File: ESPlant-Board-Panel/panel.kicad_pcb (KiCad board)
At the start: 4 copper layers, 64 x 116 mm, 150 parts, among them J1 Conn_01x05, U1 USB-C, U13 ESP32-C6-MINI-1-N4, U3 AHT20-F, U4 Tactile-Switch, U5 3.3V-Regulator, U6 Light sensor, U7 Tactile-Switch, U8 Slide-Switch, U9 Battery-Spring

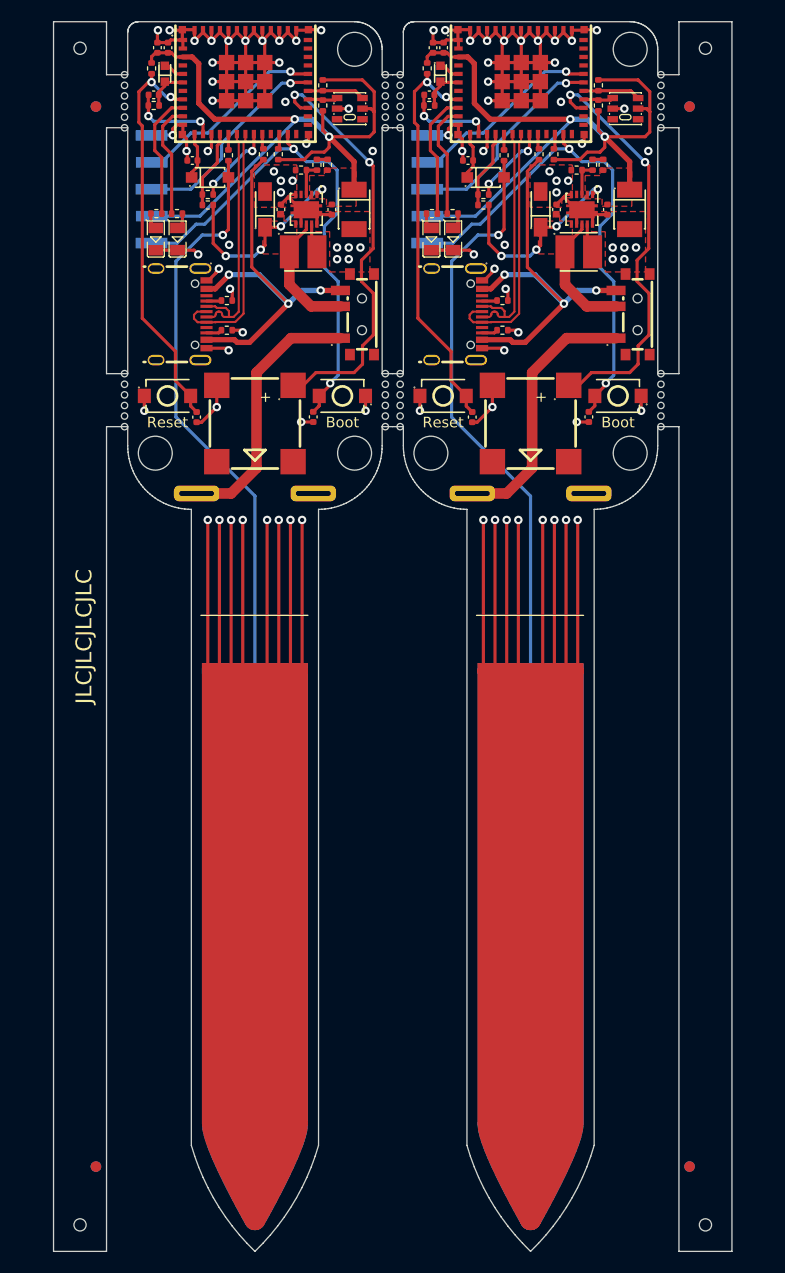
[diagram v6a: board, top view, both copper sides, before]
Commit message: Panel: Make board width be 70mm
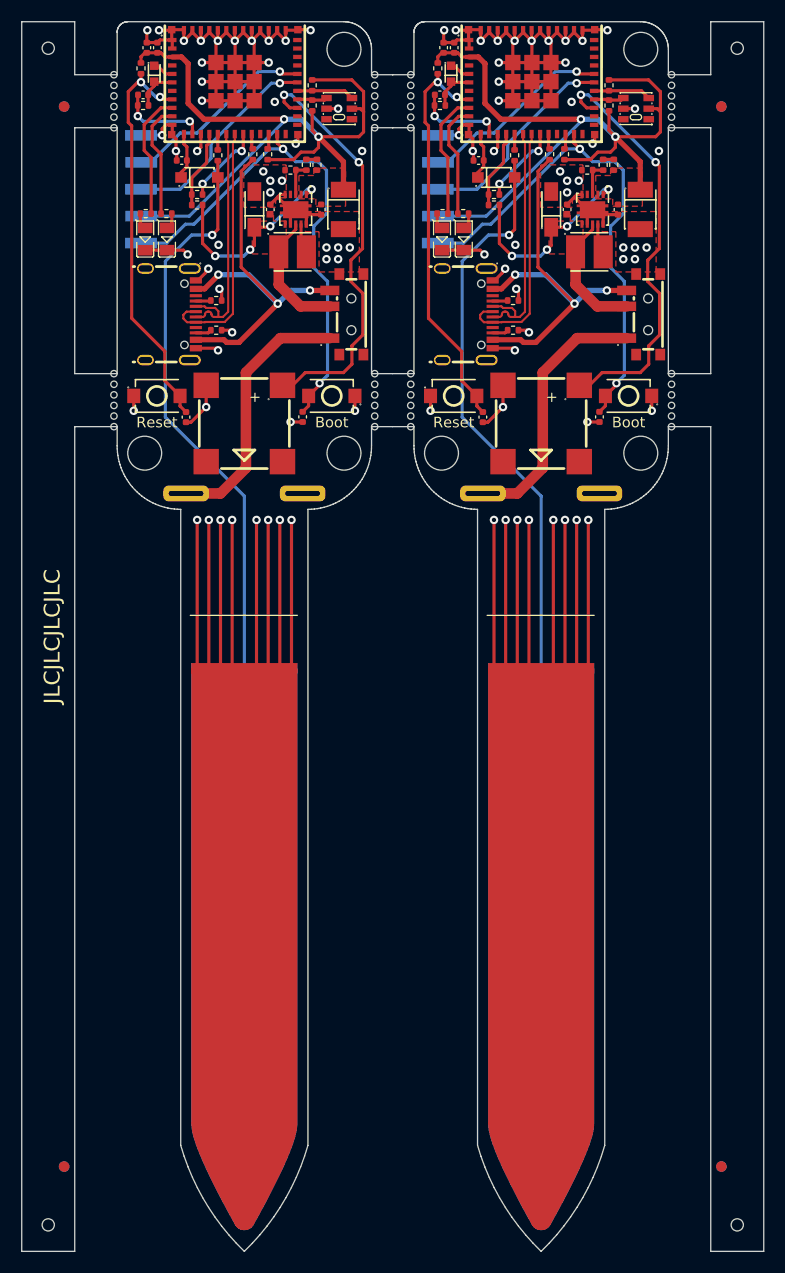
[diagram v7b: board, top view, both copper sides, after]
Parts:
- removed the BZ1 at (212.0, 57.9)
- removed the BZ1 at (238.0, 57.9)
- removed the C1 at (245.3, 37.7)
- removed the C1 at (219.3, 37.7)
- removed the C10 at (239.0, 37.7)
- removed the C10 at (213.0, 37.7)
- removed the C11 at (232.5, 57.3)
- removed the C11 at (206.5, 57.3)
- removed the C2 at (221.4, 37.7)
- removed the C2 at (247.4, 37.7)
- removed the C3 at (232.1, 33.1)
- removed the C3 at (206.1, 33.1)
- removed the C4 at (238.0, 81.0)
- removed the C4 at (212.0, 81.0)
- removed the C5 at (243.5, 57.3)
- removed the C5 at (217.5, 57.3)
- removed the C6 at (214.5, 37.7)
- removed the C6 at (240.5, 37.7)
- removed the C7 at (202.5, 26.9)
- removed the C7 at (228.5, 26.9)
- removed the C8 at (203.8, 22.4)
- removed the C8 at (229.8, 22.4)
- removed the C9 at (228.8, 22.4)
- removed the C9 at (202.8, 22.4)
- removed the D1 at (204.7, 40.5)
- removed the D1 at (230.7, 40.5)
- removed the D2 at (207.8, 34.7)
- removed the D2 at (233.8, 34.7)
- removed the D3 at (228.7, 40.5)
- removed the D3 at (202.7, 40.5)
- removed the H1 at (221.4, 22.6)
- removed the H1 at (247.4, 22.6)
- removed the H2 at (228.6, 60.7)
- removed the H2 at (202.6, 60.7)
- removed the H3 at (247.4, 60.7)
- removed the H3 at (221.4, 60.7)
- removed the J1 at (227.0, 35.8)
- removed the J1 at (201.0, 35.8)
- removed the L1 at (216.6, 41.7)
- removed the L1 at (242.6, 41.7)
- removed the R1 at (244.9, 33.5)
- removed the R1 at (218.9, 33.5)
- removed the R10 at (244.4, 27.9)
- removed the R10 at (218.4, 27.9)
- removed the R11 at (209.4, 46.3)
- removed the R11 at (235.4, 46.3)
- removed the R12 at (235.4, 49.1)
- removed the R12 at (209.4, 49.1)
- removed the R13 at (230.7, 38.1)
- removed the R13 at (204.7, 38.1)
- removed the R14 at (202.7, 38.1)
- removed the R14 at (228.7, 38.1)
- removed the R15 at (243.9, 33.5)
- removed the R15 at (217.9, 33.5)
- removed the R16 at (216.4, 34.0)
- removed the R16 at (242.4, 34.0)
- removed the R2 at (218.4, 26.0)
- removed the R2 at (244.4, 26.0)
- removed the R3 at (202.5, 27.9)
- removed the R3 at (228.5, 27.9)
- removed the R4 at (207.6, 37.3)
- removed the R4 at (233.6, 37.3)
- removed the R5 at (240.2, 32.5)
- removed the R5 at (214.2, 32.5)
- removed the R6 at (233.6, 36.3)
- removed the R6 at (207.6, 36.3)
- removed the R7 at (238.8, 32.5)
- removed the R7 at (212.8, 32.5)
- removed the R8 at (209.5, 32.6)
- removed the R8 at (235.5, 32.6)
- removed the R9 at (228.3, 24.4)
- removed the R9 at (202.3, 24.4)
- removed the U1 at (205.1, 47.6)
- removed the U1 at (231.1, 47.6)
- removed the U13 at (237.1, 25.7)
- removed the U13 at (211.1, 25.7)
- removed the U3 at (221.0, 28.2)
- removed the U3 at (247.0, 28.2)
- removed the U4 at (229.8, 55.3)
- removed the U4 at (203.8, 55.3)
- removed the U5 at (216.9, 37.7)
- removed the U5 at (242.9, 37.7)
- removed the U6 at (229.5, 24.9)
- removed the U6 at (203.5, 24.9)
- removed the U7 at (246.3, 55.3)
- removed the U7 at (220.3, 55.3)
- removed the U8 at (221.7, 47.6)
- removed the U8 at (247.7, 47.6)
- removed the U9 at (238.0, 64.5)
- removed the U9 at (212.0, 64.5)
- added BZ1: Buzzer, CustomFootprints:BUZ-SMD_4P-L8.5-W8.5-P8.50-BR, F.Cu at (211.0, 57.9)
- added BZ1: Buzzer, CustomFootprints:BUZ-SMD_4P-L8.5-W8.5-P8.50-BR, F.Cu at (239.0, 57.9)
- added C1: 2.2uF-Ceramic, Capacitor_SMD:C_0402_1005Metric, F.Cu at (246.3, 37.7)
- added C1: 2.2uF-Ceramic, Capacitor_SMD:C_0402_1005Metric, F.Cu at (218.3, 37.7)
- added C10: 10uF-Tantalum, CustomFootprints:CAP-SMD_L3.2-W1.6-RD-C7171, F.Cu at (212.0, 37.7)
- added C10: 10uF-Tantalum, CustomFootprints:CAP-SMD_L3.2-W1.6-RD-C7171, F.Cu at (240.0, 37.7)
- added C11: 100nF-Ceramic, Capacitor_SMD:C_0402_1005Metric, F.Cu at (205.5, 57.3)
- added C11: 100nF-Ceramic, Capacitor_SMD:C_0402_1005Metric, F.Cu at (233.5, 57.3)
- added C2: 100uF-Tantalum, CustomFootprints:CASE-B_3528, F.Cu at (220.4, 37.7)
- added C2: 100uF-Tantalum, CustomFootprints:CASE-B_3528, F.Cu at (248.4, 37.7)
- added C3: 10nF, Capacitor_SMD:C_0402_1005Metric, F.Cu at (205.1, 33.1)
- added C3: 10nF, Capacitor_SMD:C_0402_1005Metric, F.Cu at (233.1, 33.1)
- added C4: 7pF-27pF, A=2.75cm^2, CustomFootprints:Sensor-Tip, B.Cu at (211.0, 81.0)
- added C4: 7pF-27pF, A=2.75cm^2, CustomFootprints:Sensor-Tip, B.Cu at (239.0, 81.0)
- added C5: 100nF-Ceramic, Capacitor_SMD:C_0402_1005Metric, F.Cu at (244.5, 57.3)
- added C5: 100nF-Ceramic, Capacitor_SMD:C_0402_1005Metric, F.Cu at (216.5, 57.3)
- added C6: 100nF-Ceramic, Capacitor_SMD:C_0402_1005Metric, F.Cu at (241.5, 37.7)
- added C6: 100nF-Ceramic, Capacitor_SMD:C_0402_1005Metric, F.Cu at (213.5, 37.7)
- added C7: 10uF, Capacitor_SMD:C_0402_1005Metric, F.Cu at (201.5, 26.9)
- added C7: 10uF, Capacitor_SMD:C_0402_1005Metric, F.Cu at (229.5, 26.9)
- added C8: 10nF, Capacitor_SMD:C_0402_1005Metric, F.Cu at (202.8, 22.4)
- added C8: 10nF, Capacitor_SMD:C_0402_1005Metric, F.Cu at (230.8, 22.4)
- added C9: 10uF, Capacitor_SMD:C_0402_1005Metric, F.Cu at (201.8, 22.4)
- added C9: 10uF, Capacitor_SMD:C_0402_1005Metric, F.Cu at (229.8, 22.4)
- added D1: GREEN, CustomFootprints:LED0805-R-RD, F.Cu at (231.7, 40.5)
- added D1: GREEN, CustomFootprints:LED0805-R-RD, F.Cu at (203.7, 40.5)
- added D2: Switching-Diode, CustomFootprints:SOD-123F_L2.7-W1.6-LS3.8-RD, F.Cu at (234.8, 34.7)
- added D2: Switching-Diode, CustomFootprints:SOD-123F_L2.7-W1.6-LS3.8-RD, F.Cu at (206.8, 34.7)
- added D3: RED, CustomFootprints:LED0805-R-RD, F.Cu at (229.7, 40.5)
- added D3: RED, CustomFootprints:LED0805-R-RD, F.Cu at (201.7, 40.5)
- added H1: MountingHole, MountingHole:MountingHole_3.2mm_M3, F.Cu at (248.4, 22.6)
- added H1: MountingHole, MountingHole:MountingHole_3.2mm_M3, F.Cu at (220.4, 22.6)
- added H2: MountingHole, MountingHole:MountingHole_3.2mm_M3, F.Cu at (201.6, 60.7)
- added H2: MountingHole, MountingHole:MountingHole_3.2mm_M3, F.Cu at (229.6, 60.7)
- added H3: MountingHole, MountingHole:MountingHole_3.2mm_M3, F.Cu at (248.4, 60.7)
- added H3: MountingHole, MountingHole:MountingHole_3.2mm_M3, F.Cu at (220.4, 60.7)
- added J1: Conn_01x05, CustomFootprints:PinHeader_1x05_P2.54mm_Vertical_SMD, B.Cu at (228.0, 35.8)
- added J1: Conn_01x05, CustomFootprints:PinHeader_1x05_P2.54mm_Vertical_SMD, B.Cu at (200.0, 35.8)
- added L1: 6.8uH, CustomFootprints:IND-SMD_L3.5-W3.0, F.Cu at (243.6, 41.7)
- added L1: 6.8uH, CustomFootprints:IND-SMD_L3.5-W3.0, F.Cu at (215.6, 41.7)
- added R1: 100k, Resistor_SMD:R_0402_1005Metric, F.Cu at (245.9, 33.5)
- added R1: 100k, Resistor_SMD:R_0402_1005Metric, F.Cu at (217.9, 33.5)
- added R10: 5k1, Resistor_SMD:R_0402_1005Metric, F.Cu at (245.4, 27.9)
- added R10: 5k1, Resistor_SMD:R_0402_1005Metric, F.Cu at (217.4, 27.9)
- added R11: 5k1, Resistor_SMD:R_0402_1005Metric, F.Cu at (208.4, 46.3)
- added R11: 5k1, Resistor_SMD:R_0402_1005Metric, F.Cu at (236.4, 46.3)
- added R12: 5k1, Resistor_SMD:R_0402_1005Metric, F.Cu at (236.4, 49.1)
- added R12: 5k1, Resistor_SMD:R_0402_1005Metric, F.Cu at (208.4, 49.1)
- added R13: 120, Resistor_SMD:R_0402_1005Metric, F.Cu at (231.7, 38.1)
- added R13: 120, Resistor_SMD:R_0402_1005Metric, F.Cu at (203.7, 38.1)
- added R14: 120, Resistor_SMD:R_0402_1005Metric, F.Cu at (201.7, 38.1)
- added R14: 120, Resistor_SMD:R_0402_1005Metric, F.Cu at (229.7, 38.1)
- added R15: 1M, Resistor_SMD:R_0402_1005Metric, F.Cu at (244.9, 33.5)
- added R15: 1M, Resistor_SMD:R_0402_1005Metric, F.Cu at (216.9, 33.5)
- added R16: 200k, Resistor_SMD:R_0402_1005Metric, F.Cu at (215.4, 34.0)
- added R16: 200k, Resistor_SMD:R_0402_1005Metric, F.Cu at (243.4, 34.0)
- added R2: 5k1, Resistor_SMD:R_0402_1005Metric, F.Cu at (217.4, 26.0)
- added R2: 5k1, Resistor_SMD:R_0402_1005Metric, F.Cu at (245.4, 26.0)
- added R3: 47k, Resistor_SMD:R_0402_1005Metric, F.Cu at (229.5, 27.9)
- added R3: 47k, Resistor_SMD:R_0402_1005Metric, F.Cu at (201.5, 27.9)
- added R4: 5k1, Resistor_SMD:R_0402_1005Metric, F.Cu at (234.6, 37.3)
- added R4: 5k1, Resistor_SMD:R_0402_1005Metric, F.Cu at (206.6, 37.3)
- added R5: 10k, Resistor_SMD:R_0402_1005Metric, F.Cu at (213.2, 32.5)
- added R5: 10k, Resistor_SMD:R_0402_1005Metric, F.Cu at (241.2, 32.5)
- added R6: 2k, Resistor_SMD:R_0402_1005Metric, F.Cu at (234.6, 36.3)
- added R6: 2k, Resistor_SMD:R_0402_1005Metric, F.Cu at (206.6, 36.3)
- added R7: 10k, Resistor_SMD:R_0402_1005Metric, F.Cu at (211.8, 32.5)
- added R7: 10k, Resistor_SMD:R_0402_1005Metric, F.Cu at (239.8, 32.5)
- added R8: 10k, Resistor_SMD:R_0402_1005Metric, F.Cu at (208.5, 32.6)
- added R8: 10k, Resistor_SMD:R_0402_1005Metric, F.Cu at (236.5, 32.6)
- added R9: 10k, Resistor_SMD:R_0402_1005Metric, F.Cu at (229.3, 24.4)
- added R9: 10k, Resistor_SMD:R_0402_1005Metric, F.Cu at (201.3, 24.4)
- added U1: USB-C, CustomFootprints:USB-C-SMD_G-SWITCH_GT-USB-7010EN, F.Cu at (232.1, 47.6)
- added U1: USB-C, CustomFootprints:USB-C-SMD_G-SWITCH_GT-USB-7010EN, F.Cu at (204.1, 47.6)
- added U13: ESP32-C6-MINI-1-N4, CustomFootprints:WIFIM-SMD_61P-L16.6-W13.2-P0.80-ESP32-C6-MINI-1-N4, F.Cu at (238.1, 25.7)
- added U13: ESP32-C6-MINI-1-N4, CustomFootprints:WIFIM-SMD_61P-L16.6-W13.2-P0.80-ESP32-C6-MINI-1-N4, F.Cu at (210.1, 25.7)
- added U3: AHT20-F, CustomFootprints:SENSOR-SMD-6_AHT20, F.Cu at (220.0, 28.2)
- added U3: AHT20-F, CustomFootprints:SENSOR-SMD-6_AHT20, F.Cu at (248.0, 28.2)
- added U4: Tactile-Switch, CustomFootprints:SW-SMD_L3.9-W3.0-P4.45, F.Cu at (230.8, 55.3)
- added U4: Tactile-Switch, CustomFootprints:SW-SMD_L3.9-W3.0-P4.45, F.Cu at (202.8, 55.3)
- added U5: 3.3V-Regulator, CustomFootprints:VSON-10_L3.0-W3.0-P0.50-BL-EP_TPS62410DRCR, F.Cu at (215.9, 37.7)
- added U5: 3.3V-Regulator, CustomFootprints:VSON-10_L3.0-W3.0-P0.50-BL-EP_TPS62410DRCR, F.Cu at (243.9, 37.7)
- added U6: Light sensor, CustomFootprints:SENSORS-SMD_ALS-PT19, F.Cu at (202.5, 24.9)
- added U6: Light sensor, CustomFootprints:SENSORS-SMD_ALS-PT19, F.Cu at (230.5, 24.9)
- added U7: Tactile-Switch, CustomFootprints:SW-SMD_L3.9-W3.0-P4.45, F.Cu at (247.3, 55.3)
- added U7: Tactile-Switch, CustomFootprints:SW-SMD_L3.9-W3.0-P4.45, F.Cu at (219.3, 55.3)
- added U8: Slide-Switch, CustomFootprints:SW-SMD_MK-12C02-G025, F.Cu at (220.7, 47.6)
- added U8: Slide-Switch, CustomFootprints:SW-SMD_MK-12C02-G025, F.Cu at (248.7, 47.6)
- added U9: Battery-Spring, CustomFootprints:AAA Battery-spring, B.Cu at (239.0, 64.5)
- added U9: Battery-Spring, CustomFootprints:AAA Battery-spring, B.Cu at (211.0, 64.5)
- moved KiKit_FID_B_2 3.00 mm to (256.0, 28.0)
- moved KiKit_FID_B_4 3.00 mm to (256.0, 128.0)
- moved KiKit_FID_T_2 3.00 mm to (256.0, 28.0)
- moved KiKit_FID_T_4 3.00 mm to (256.0, 128.0)
- moved KiKit_TO_2 3.00 mm to (257.5, 22.5)
- moved KiKit_TO_4 3.00 mm to (257.5, 133.5)
- moved KiKit_FID_B_1 3.00 mm to (194.0, 28.0)
- moved KiKit_FID_B_3 3.00 mm to (194.0, 128.0)
- moved KiKit_FID_T_1 3.00 mm to (194.0, 28.0)
- moved KiKit_FID_T_3 3.00 mm to (194.0, 128.0)
- moved KiKit_TO_1 3.00 mm to (192.5, 22.5)
- moved KiKit_TO_3 3.00 mm to (192.5, 133.5)
- moved KiKit_MB_1_1 1.00 mm to (223.3, 58.2)
- moved KiKit_MB_1_2 1.00 mm to (223.3, 57.2)
- moved KiKit_MB_1_3 1.00 mm to (223.3, 56.2)
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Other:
- board size 64 x 116 mm -> 70 x 116 mm

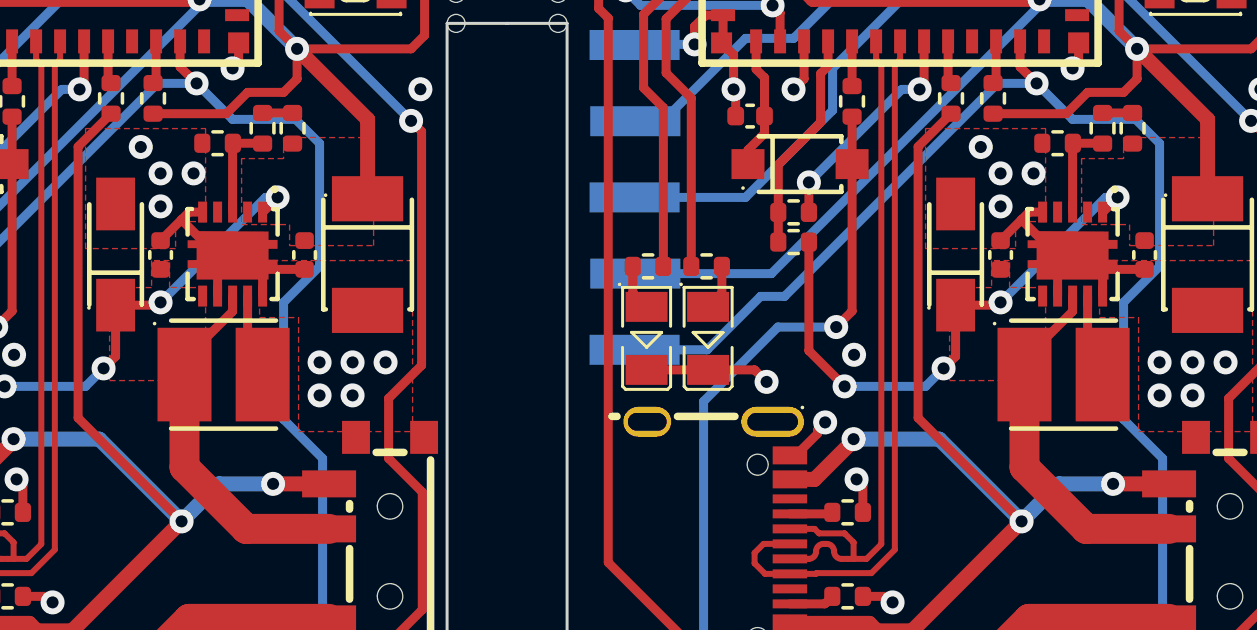
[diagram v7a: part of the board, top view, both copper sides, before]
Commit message: Board: Enable Power saving mode
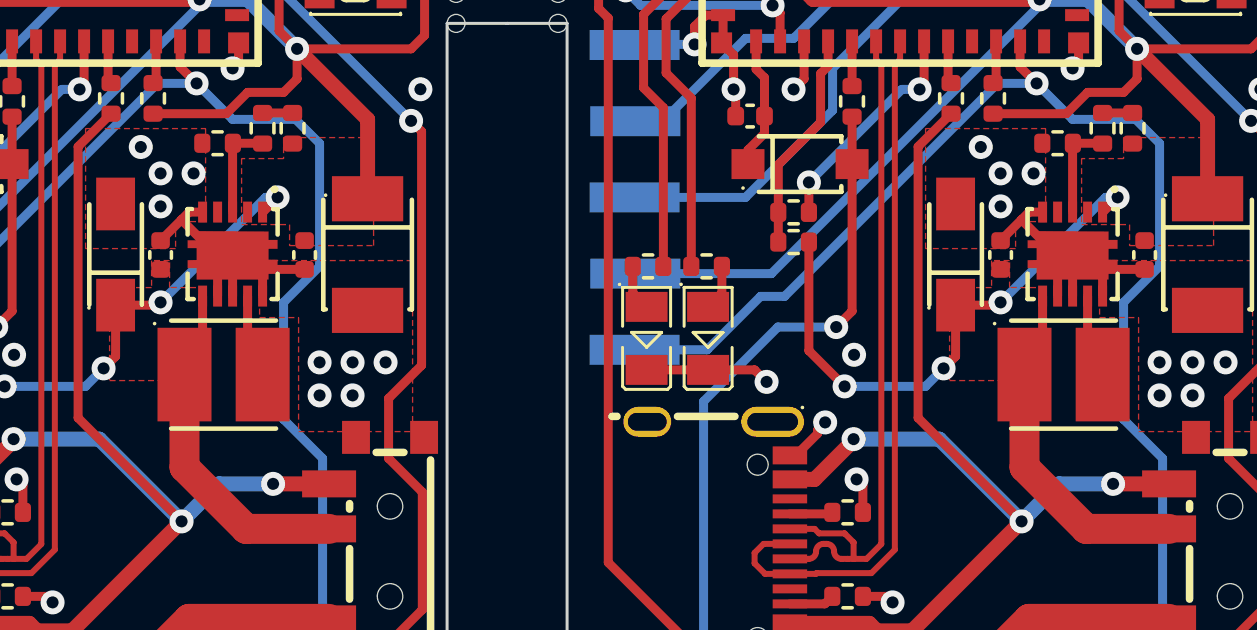
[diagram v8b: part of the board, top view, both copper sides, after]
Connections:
- U5 pad 8: Board_1-PWR_VIN -> Board_1-GND
- U5 pad 8: Board_0-PWR_VIN -> Board_0-GND
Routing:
- net Board_0-GND: track 218.5 -> 219.9 mm
- net Board_1-GND: track 218.5 -> 219.9 mm
